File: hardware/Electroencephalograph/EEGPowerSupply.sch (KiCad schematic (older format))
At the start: 25 parts, among them U10 TC1017-xCT, U11 TPS60403, U8 TC1017-xCT, U9 TC1017-xCT

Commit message: enqable separate electrodes for each point
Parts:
- added C62: 100n, Capacitor_SMD:C_0402_1005Metric, symbol Device:C
- added L4, L5: 3u3, Inductor_SMD:L_1206_3216Metric, symbol Device:L
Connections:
- wire segments 85 -> 90
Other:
- moved on the sheet: C71, TP4, TP6
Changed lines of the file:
@@
 $Descr A4 11693 8268
 encoding utf-8
-Sheet 6 6
+Sheet 6 7
 Title ""
 Date ""
@@
 AR Path="/5DFE0AD6/5E0A0C58" Ref="U?"  Part="1"
 AR Path="/5E0992D6/5E0A0C58" Ref="U11"  Part="1"
-F 0 "U11" H 3750 5750 50  0000 L CNN
-F 1 "TPS60403" H 3650 5650 50  0000 L CNN
+F 0 "U11" H 3550 5800 50  0000 L CNN
+F 1 "TPS60403" H 3550 5700 50  0000 L CNN
 F 2 "Package_SO:SOP-8_3.76x4.96mm_P1.27mm" H 5050 5650 50  0001 C CNN
 F 3 "" H 5050 5650 50  0001 C CNN
@@
 L Device:CP C?
 U 1 1 5E0A0CA0
-P 4250 5200
+P 4400 5200
 AR Path="/5DF4CFF8/5E0A0CA0" Ref="C?"  Part="1"
 AR Path="/5DF61103/5E0A0CA0" Ref="C?"  Part="1"
 AR Path="/5DFE0AD6/5E0A0CA0" Ref="C?"  Part="1"
 AR Path="/5E0992D6/5E0A0CA0" Ref="C71"  Part="1"
-F 0 "C71" H 4368 5246 50  0000 L CNN
-F 1 "22u" H 4368 5155 50  0000 L CNN
-F 2 "Capacitor_Tantalum_SMD:CP_EIA-3528-21_Kemet-B" H 4288 5050 50  0001 C CNN
-F 3 "~" H 4250 5200 50  0001 C CNN
-	1    4250 5200
+F 0 "C71" H 4518 5246 50  0000 L CNN
+F 1 "22u" H 4518 5155 50  0000 L CNN
+F 2 "Capacitor_Tantalum_SMD:CP_EIA-3528-21_Kemet-B" H 4438 5050 50  0001 C CNN
+F 3 "~" H 4400 5200 50  0001 C CNN
+	1    4400 5200
 	1    0    0    1
 $EndComp
@@
 Connection ~ 2700 5500
 Wire Wire Line
-	3850 5500 4250 5500
-Wire Wire Line
-	4250 5500 4250 5350
-Connection ~ 3850 5500
+	4400 5500 4400 5350
 $Comp
 L Electroencephalograph:A_GND #PWR?
 U 1 1 5E0A0CB3
-P 4250 5000
+P 4400 5000
 AR Path="/5DFE0AD6/5E0A0CB3" Ref="#PWR?"  Part="1"
 AR Path="/5E0992D6/5E0A0CB3" Ref="#PWR117"  Part="1"
-F 0 "#PWR117" H 4250 5025 50  0001 C CNN
-F 1 "A_GND" H 4267 4827 50  0000 C CNN
-F 2 "" H 4250 5025 50  0001 C CNN
-F 3 "" H 4250 5025 50  0001 C CNN
-	1    4250 5000
-	1    0    0    1
-$EndComp
-Wire Wire Line
-	4250 5000 4250 5050
+F 0 "#PWR117" H 4400 5025 50  0001 C CNN
+F 1 "A_GND" H 4417 4827 50  0000 C CNN
+F 2 "" H 4400 5025 50  0001 C CNN
+F 3 "" H 4400 5025 50  0001 C CNN
+	1    4400 5000
+	1    0    0    1
+$EndComp
+Wire Wire Line
+	4400 5000 4400 5050
 $Comp
 L Device:C C?
@@
 	6550 5000 6550 5100
 Wire Wire Line
-	4250 5500 5350 5500
-Connection ~ 4250 5500
+	4400 5500 5350 5500
+Connection ~ 4400 5500
 Wire Wire Line
 	6550 5500 6550 5400
@@
 $EndComp
 $Comp
-L Device:C C?
-U 1 1 5E104488
-P 6600 2750
-AR Path="/5DF4CFF8/5E104488" Ref="C?"  Part="1"
-AR Path="/5DF61103/5E104488" Ref="C?"  Part="1"
-AR Path="/5DFE0AD6/5E104488" Ref="C?"  Part="1"
-AR Path="/5E0992D6/5E104488" Ref="C61"  Part="1"
-F 0 "C61" H 6715 2796 50  0000 L CNN
-F 1 "1u" H 6715 2705 50  0000 L CNN
-F 2 "Capacitor_SMD:C_0402_1005Metric" H 6638 2600 50  0001 C CNN
-F 3 "~" H 6600 2750 50  0001 C CNN
-	1    6600 2750
-	1    0    0    -1
-$EndComp
-$Comp
 L Electroencephalograph:D_GND #PWR?
 U 1 1 5E10486F
@@
 	1    0    0    -1
 $EndComp
-$Comp
-L Electroencephalograph:D_GND #PWR?
-U 1 1 5E108919
-P 6600 3000
-AR Path="/5DFE0AD6/5E108919" Ref="#PWR?"  Part="1"
-AR Path="/5E0992D6/5E108919" Ref="#PWR107"  Part="1"
-F 0 "#PWR107" H 6600 3025 50  0001 C CNN
-F 1 "D_GND" H 6617 2827 50  0000 C CNN
-F 2 "" H 6600 3025 50  0001 C CNN
-F 3 "" H 6600 3025 50  0001 C CNN
-	1    6600 3000
-	1    0    0    -1
-$EndComp
 Wire Wire Line
 	5500 2400 5350 2400
@@
 	6000 2800 6000 3000
 Wire Wire Line
-	6400 2400 6600 2400
-Wire Wire Line
-	6600 2400 6600 2600
-Wire Wire Line
-	6600 2900 6600 3000
-Wire Wire Line
-	6600 2400 8300 2400
-Wire Wire Line
 	8300 2400 8300 2250
-Connection ~ 6600 2400
 Wire Wire Line
 	5350 2400 2050 2400
@@
 L Connector:TestPoint TP?
 U 1 1 5E19CD08
-P 6600 2300
+P 7100 2300
 AR Path="/5DF61103/5E19CD08" Ref="TP?"  Part="1"
 AR Path="/5E0992D6/5E19CD08" Ref="TP4"  Part="1"
-F 0 "TP4" H 6658 2418 50  0000 L CNN
-F 1 "TestPoint" H 6658 2327 50  0000 L CNN
-F 2 "TestPoint:TestPoint_Pad_1.5x1.5mm" H 6800 2300 50  0001 C CNN
-F 3 "~" H 6800 2300 50  0001 C CNN
-	1    6600 2300
-	1    0    0    -1
-$EndComp
-Wire Wire Line
-	6600 2300 6600 2400
+F 0 "TP4" H 7158 2418 50  0000 L CNN
+F 1 "TestPoint" H 7158 2327 50  0000 L CNN
+F 2 "TestPoint:TestPoint_Pad_1.5x1.5mm" H 7300 2300 50  0001 C CNN
+F 3 "~" H 7300 2300 50  0001 C CNN
+	1    7100 2300
+	1    0    0    -1
+$EndComp
 $Comp
 L Connector:TestPoint TP?
@@
 L Connector:TestPoint TP?
 U 1 1 5E1AE8F5
-P 4250 5600
+P 4400 5600
 AR Path="/5DF61103/5E1AE8F5" Ref="TP?"  Part="1"
 AR Path="/5E0992D6/5E1AE8F5" Ref="TP6"  Part="1"
-F 0 "TP6" H 4192 5626 50  0000 R CNN
-F 1 "TestPoint" H 4192 5717 50  0000 R CNN
-F 2 "TestPoint:TestPoint_Pad_1.5x1.5mm" H 4450 5600 50  0001 C CNN
-F 3 "~" H 4450 5600 50  0001 C CNN
-	1    4250 5600
+F 0 "TP6" H 4342 5626 50  0000 R CNN
+F 1 "TestPoint" H 4342 5717 50  0000 R CNN
+F 2 "TestPoint:TestPoint_Pad_1.5x1.5mm" H 4600 5600 50  0001 C CNN
+F 3 "~" H 4600 5600 50  0001 C CNN
+	1    4400 5600
 	-1   0    0    1
 $EndComp
 Wire Wire Line
-	4250 5600 4250 5500
+	4400 5600 4400 5500
+$Comp
+L Device:L L?
+U 1 1 5DFF5B3E
+P 4100 5500
+AR Path="/5DFE0AD6/5DFF5B3E" Ref="L?"  Part="1"
+AR Path="/5E0992D6/5DFF5B3E" Ref="L5"  Part="1"
+F 0 "L5" V 4290 5500 50  0000 C CNN
+F 1 "3u3" V 4199 5500 50  0000 C CNN
+F 2 "Inductor_SMD:L_1206_3216Metric" H 4100 5500 50  0001 C CNN
+F 3 "~" H 4100 5500 50  0001 C CNN
+	1    4100 5500
+	0    1    1    0
+$EndComp
+$Comp
+L Device:C C?
+U 1 1 5DFFE643
+P 6550 2650
+AR Path="/5DF4CFF8/5DFFE643" Ref="C?"  Part="1"
+AR Path="/5DF61103/5DFFE643" Ref="C?"  Part="1"
+AR Path="/5DFE0AD6/5DFFE643" Ref="C?"  Part="1"
+AR Path="/5E0992D6/5DFFE643" Ref="C61"  Part="1"
+F 0 "C61" H 6665 2696 50  0000 L CNN
+F 1 "1u" H 6665 2605 50  0000 L CNN
+F 2 "Capacitor_SMD:C_0402_1005Metric" H 6588 2500 50  0001 C CNN
+F 3 "~" H 6550 2650 50  0001 C CNN
+	1    6550 2650
+	1    0    0    -1
+$EndComp
+$Comp
+L Electroencephalograph:A_GND #PWR?
+U 1 1 5DFFE649
+P 6550 2900
+AR Path="/5DFE0AD6/5DFFE649" Ref="#PWR?"  Part="1"
+AR Path="/5E0992D6/5DFFE649" Ref="#PWR107"  Part="1"
+F 0 "#PWR107" H 6550 2925 50  0001 C CNN
+F 1 "A_GND" H 6567 2727 50  0000 C CNN
+F 2 "" H 6550 2925 50  0001 C CNN
+F 3 "" H 6550 2925 50  0001 C CNN
+	1    6550 2900
+	1    0    0    -1
+$EndComp
+Wire Wire Line
+	6550 2900 6550 2800
+Wire Wire Line
+	6550 2400 6550 2500
+$Comp
+L Device:L L?
+U 1 1 5DFFE651
+P 6850 2400
+AR Path="/5DFE0AD6/5DFFE651" Ref="L?"  Part="1"
+AR Path="/5E0992D6/5DFFE651" Ref="L4"  Part="1"
+F 0 "L4" V 7040 2400 50  0000 C CNN
+F 1 "3u3" V 6949 2400 50  0000 C CNN
+F 2 "Inductor_SMD:L_1206_3216Metric" H 6850 2400 50  0001 C CNN
+F 3 "~" H 6850 2400 50  0001 C CNN
+	1    6850 2400
+	0    -1   -1   0
+$EndComp
+$Comp
+L Device:C C?
+U 1 1 5DFFE657
+P 7100 2650
+AR Path="/5DF4CFF8/5DFFE657" Ref="C?"  Part="1"
+AR Path="/5DF61103/5DFFE657" Ref="C?"  Part="1"
+AR Path="/5DFE0AD6/5DFFE657" Ref="C?"  Part="1"
+AR Path="/5E0992D6/5DFFE657" Ref="C62"  Part="1"
+F 0 "C62" H 7215 2696 50  0000 L CNN
+F 1 "100n" H 7215 2605 50  0000 L CNN
+F 2 "Capacitor_SMD:C_0402_1005Metric" H 7138 2500 50  0001 C CNN
+F 3 "~" H 7100 2650 50  0001 C CNN
+	1    7100 2650
+	1    0    0    -1
+$EndComp
+Wire Wire Line
+	6550 2400 6700 2400
+Connection ~ 6550 2400
+Wire Wire Line
+	7000 2400 7100 2400
+Wire Wire Line
+	7100 2400 7100 2500
+$Comp
+L Electroencephalograph:A_GND #PWR?
+U 1 1 5DFFE661
+P 7100 2900
+AR Path="/5DFE0AD6/5DFFE661" Ref="#PWR?"  Part="1"
+AR Path="/5E0992D6/5DFFE661" Ref="#PWR121"  Part="1"
+F 0 "#PWR121" H 7100 2925 50  0001 C CNN
+F 1 "A_GND" H 7117 2727 50  0000 C CNN
+F 2 "" H 7100 2925 50  0001 C CNN
+F 3 "" H 7100 2925 50  0001 C CNN
+	1    7100 2900
+	1    0    0    -1
+$EndComp
+Wire Wire Line
+	7100 2900 7100 2800
+Connection ~ 7100 2400
+Wire Wire Line
+	6400 2400 6550 2400
+Wire Wire Line
+	7100 2400 8300 2400
+Wire Wire Line
+	7100 2300 7100 2400
+Wire Wire Line
+	3850 5500 3950 5500
+Connection ~ 3850 5500
+Wire Wire Line
+	4250 5500 4400 5500
 $EndSCHEMATC

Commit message: removed external clk and vref
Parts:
- removed L2, L3, L4: 3u3, Inductor_SMD:L_1206_3216Metric, symbol Device:L
- removed U10, U8, U9: TC1017-xCT, Package_TO_SOT_SMD:SOT-23-5, symbol Regulator_Linear:TC1017-xCT
- added L5: 22u, Inductor_SMD:L_1206_3216Metric, symbol Device:L
- added TP8: TestPoint, TestPoint:TestPoint_Pad_1.5x1.5mm, symbol Connector:TestPoint
- added U6, U7, U9: LP5912-1.8DRVT, symbol Electroencephalograph:LP5912-1.8DRVT
- C56: renamed from C61; value 1u -> 2u2
- C58: renamed from C60; value 1u -> 2u2
- C59: renamed from C63; value 1u -> 2u2
- C61: renamed from C64; value 1u -> 2u2
- C66: renamed from C72; value 1u -> 2u2
- C68: renamed from C67; value 22u -> 100u
- C69: value 1u -> 2u2
- L6: renamed from L5; value 3u3 -> 22u
- renumbered C62 to C57, C55 to C60, C57 to C62, C58 to C63, C70 to C64, C71 to C65, C68 to C67, C59 to C70, C65 to C71, TP5 to TP10, TP6 to TP11, TP7 to TP12, TP4 to TP9, U11 to U8
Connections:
- wire segments 90 -> 107
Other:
- note added: "Power Supply (TP8) = 5V\nD_VDD (TP9) = 1V8\nA_VDD (TP10) = 1V8\nA_VSS (TP12) = -1V8\nvoltage inverter output (TP11) =-4V5"
- moved on the sheet: C56, C57, C58, C59, C60, C61, C62, C63, C64, C65, C66, C67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

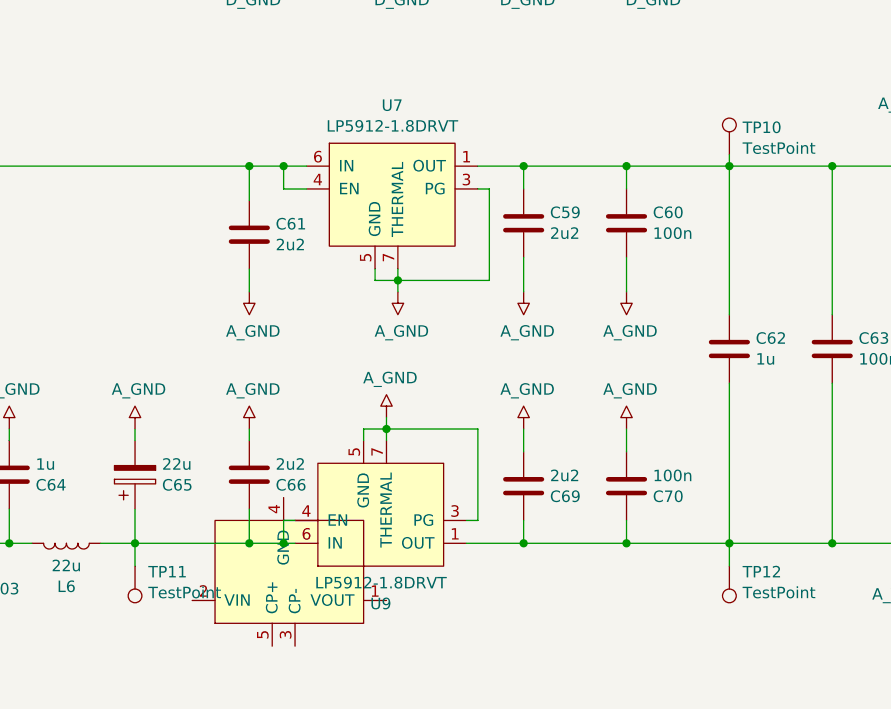
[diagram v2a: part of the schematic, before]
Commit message: bom simplification
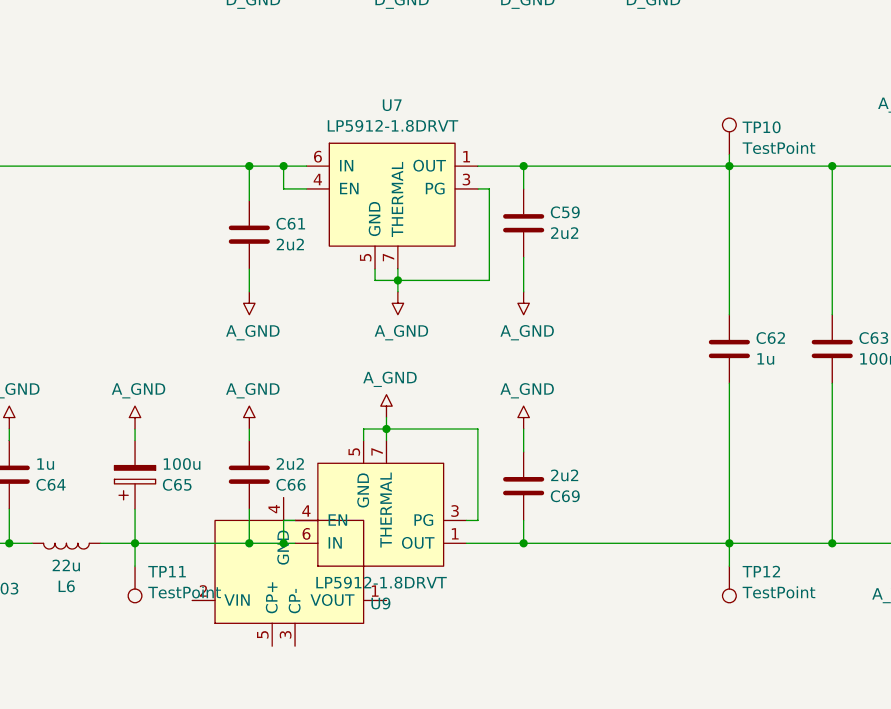
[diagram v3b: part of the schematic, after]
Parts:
- removed C60, C70: 100n, Capacitor_SMD:C_0402_1005Metric, symbol Device:C
- C65: value 22u -> 100u
- C68: footprint Capacitor_Tantalum_SMD:CP_EIA-3528-21_Kemet-B -> Capacitor_SMD:CP_Elec_6.3x5.8
- L5, L6: footprint Inductor_SMD:L_1206_3216Metric -> Inductor_SMD:L_7.3x7.3_H3.5
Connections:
- wire segments 107 -> 101
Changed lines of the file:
@@
 F 0 "C68" H 2882 5296 50  0000 R CNN
 F 1 "100u" H 2882 5205 50  0000 R CNN
-F 2 "Capacitor_Tantalum_SMD:CP_EIA-3528-21_Kemet-B" H 3038 5100 50  0001 C CNN
+F 2 "Capacitor_SMD:CP_Elec_6.3x5.8" H 3038 5100 50  0001 C CNN
 F 3 "~" H 3000 5250 50  0001 C CNN
 	1    3000 5250
@@
 AR Path="/5E0992D6/5E0A0CA0" Ref="C65"  Part="1"
 F 0 "C65" H 4918 5246 50  0000 L CNN
-F 1 "22u" H 4918 5155 50  0000 L CNN
+F 1 "100u" H 4918 5155 50  0000 L CNN
 F 2 "Capacitor_Tantalum_SMD:CP_EIA-3528-21_Kemet-B" H 4838 5050 50  0001 C CNN
 F 3 "~" H 4800 5200 50  0001 C CNN
@@
 	1    0    0    -1
 $EndComp
-$Comp
-L Device:C C?
-U 1 1 5E0CDD1B
-P 6950 4100
-AR Path="/5DF4CFF8/5E0CDD1B" Ref="C?"  Part="1"
-AR Path="/5DF61103/5E0CDD1B" Ref="C?"  Part="1"
-AR Path="/5DFE0AD6/5E0CDD1B" Ref="C?"  Part="1"
-AR Path="/5E0992D6/5E0CDD1B" Ref="C60"  Part="1"
-F 0 "C60" H 7065 4146 50  0000 L CNN
-F 1 "100n" H 7065 4055 50  0000 L CNN
-F 2 "Capacitor_SMD:C_0402_1005Metric" H 6988 3950 50  0001 C CNN
-F 3 "~" H 6950 4100 50  0001 C CNN
-	1    6950 4100
-	1    0    0    -1
-$EndComp
 Connection ~ 6500 3850
-Wire Wire Line
-	6950 3850 6950 3950
-$Comp
-L Electroencephalograph:A_GND #PWR?
-U 1 1 5E0CF637
-P 6950 4400
-AR Path="/5DFE0AD6/5E0CF637" Ref="#PWR?"  Part="1"
-AR Path="/5E0992D6/5E0CF637" Ref="#PWR117"  Part="1"
-F 0 "#PWR117" H 6950 4425 50  0001 C CNN
-F 1 "A_GND" H 6967 4227 50  0000 C CNN
-F 2 "" H 6950 4425 50  0001 C CNN
-F 3 "" H 6950 4425 50  0001 C CNN
-	1    6950 4400
-	1    0    0    -1
-$EndComp
-Wire Wire Line
-	6950 4400 6950 4250
-Wire Wire Line
-	6950 3850 7400 3850
-Connection ~ 6950 3850
-$Comp
-L Device:C C?
-U 1 1 5E0D898C
-P 6950 5250
-AR Path="/5DF4CFF8/5E0D898C" Ref="C?"  Part="1"
-AR Path="/5DF61103/5E0D898C" Ref="C?"  Part="1"
-AR Path="/5DFE0AD6/5E0D898C" Ref="C?"  Part="1"
-AR Path="/5E0992D6/5E0D898C" Ref="C70"  Part="1"
-F 0 "C70" H 7065 5296 50  0000 L CNN
-F 1 "100n" H 7065 5205 50  0000 L CNN
-F 2 "Capacitor_SMD:C_0402_1005Metric" H 6988 5100 50  0001 C CNN
-F 3 "~" H 6950 5250 50  0001 C CNN
-	1    6950 5250
-	1    0    0    1
-$EndComp
-Wire Wire Line
-	6950 5500 6950 5400
-$Comp
-L Electroencephalograph:A_GND #PWR?
-U 1 1 5E0D8994
-P 6950 5000
-AR Path="/5DFE0AD6/5E0D8994" Ref="#PWR?"  Part="1"
-AR Path="/5E0992D6/5E0D8994" Ref="#PWR126"  Part="1"
-F 0 "#PWR126" H 6950 5025 50  0001 C CNN
-F 1 "A_GND" H 6967 4827 50  0000 C CNN
-F 2 "" H 6950 5025 50  0001 C CNN
-F 3 "" H 6950 5025 50  0001 C CNN
-	1    6950 5000
-	1    0    0    1
-$EndComp
-Wire Wire Line
-	6950 5000 6950 5100
-Wire Wire Line
-	6950 5500 7400 5500
 Wire Wire Line
 	7400 3850 7850 3850
@@
 F 0 "L6" V 4690 5500 50  0000 C CNN
 F 1 "22u" V 4599 5500 50  0000 C CNN
-F 2 "Inductor_SMD:L_1206_3216Metric" H 4500 5500 50  0001 C CNN
+F 2 "Inductor_SMD:L_7.3x7.3_H3.5" H 4500 5500 50  0001 C CNN
 F 3 "~" H 4500 5500 50  0001 C CNN
 	1    4500 5500
@@
 F 0 "L5" V 2890 5500 50  0000 C CNN
 F 1 "22u" V 2799 5500 50  0000 C CNN
-F 2 "Inductor_SMD:L_1206_3216Metric" H 2700 5500 50  0001 C CNN
+F 2 "Inductor_SMD:L_7.3x7.3_H3.5" H 2700 5500 50  0001 C CNN
 F 3 "~" H 2700 5500 50  0001 C CNN
 	1    2700 5500
@@
 	2850 5500 3000 5500
 Connection ~ 3000 5500
-Wire Wire Line
-	6500 3850 6950 3850
 Wire Wire Line
 	6500 2400 7050 2400
@@
 Wire Wire Line
 	6250 5500 6500 5500
-Wire Wire Line
-	6500 5500 6950 5500
 Connection ~ 6500 5500
-Connection ~ 6950 5500
 $Comp
 L Connector:TestPoint TP?
@@
 	2400 2050 2400 1950
 Connection ~ 2050 2050
+Wire Wire Line
+	6500 5500 7400 5500
+Wire Wire Line
+	6500 3850 7400 3850
 $EndSCHEMATC

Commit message: draft of PCB routing
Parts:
- renumbered C67 to C56, C68 to C57, C71 to C58, C64 to C59, C65 to C60, C58 to C61, C61 to C62, C66 to C63, C56 to C64, C59 to C65, C69 to C66, C57 to C67, C62 to C68, C63 to C69, TP11 to TP10, TP9 to TP11, TP10 to TP12, TP12 to TP13, TP8 to TP9, U8 to U6, U9 to U7, U6 to U8, U7 to U9

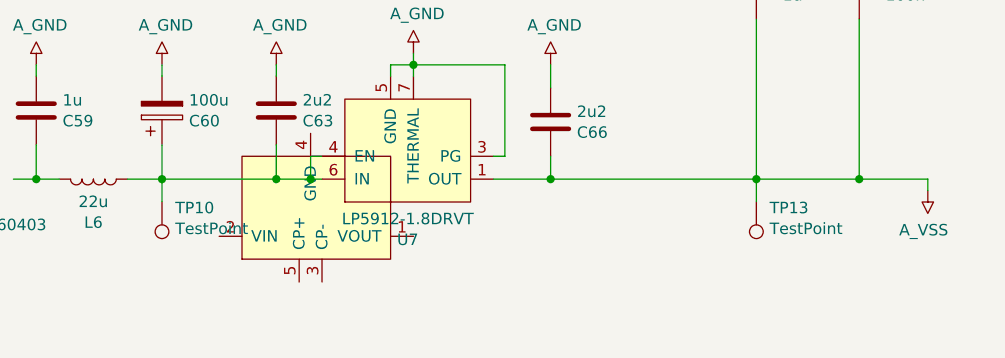
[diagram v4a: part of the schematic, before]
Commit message: added inductor 3d model
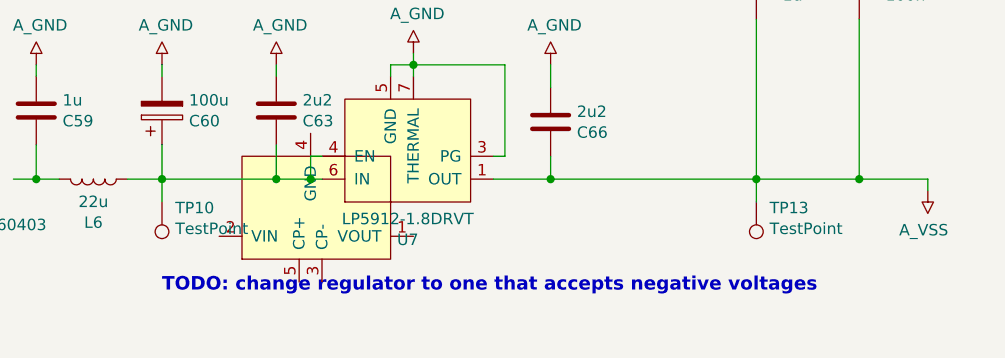
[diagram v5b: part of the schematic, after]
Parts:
- L5, L6: footprint Inductor_SMD:L_7.3x7.3_H3.5 -> Electroencephalograph:L_7.3x7.3_H3.5
- U7, U8, U9: footprint (none) -> Package_SON:WSON-8-1EP_2x2mm_P0.5mm_EP0.9x1.6mm_ThermalVias
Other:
- note added: "TODO: change regulator to one that accepts negative voltages"
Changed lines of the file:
@@
 F 0 "L6" V 4690 5500 50  0000 C CNN
 F 1 "22u" V 4599 5500 50  0000 C CNN
-F 2 "Inductor_SMD:L_7.3x7.3_H3.5" H 4500 5500 50  0001 C CNN
+F 2 "Electroencephalograph:L_7.3x7.3_H3.5" H 4500 5500 50  0001 C CNN
 F 3 "~" H 4500 5500 50  0001 C CNN
 	1    4500 5500
@@
 F 0 "L5" V 2890 5500 50  0000 C CNN
 F 1 "22u" V 2799 5500 50  0000 C CNN
-F 2 "Inductor_SMD:L_7.3x7.3_H3.5" H 2700 5500 50  0001 C CNN
+F 2 "Electroencephalograph:L_7.3x7.3_H3.5" H 2700 5500 50  0001 C CNN
 F 3 "~" H 2700 5500 50  0001 C CNN
 	1    2700 5500
@@
 F 0 "U8" H 5925 2365 50  0000 C CNN
 F 1 "LP5912-1.8DRVT" H 5925 2274 50  0000 C CNN
-F 2 "" H 5950 2250 50  0001 C CNN
+F 2 "Package_SON:WSON-8-1EP_2x2mm_P0.5mm_EP0.9x1.6mm_ThermalVias" H 5950 2250 50  0001 C CNN
 F 3 "" H 5950 2250 50  0001 C CNN
 	1    5950 2250
@@
 F 0 "U9" H 5925 3815 50  0000 C CNN
 F 1 "LP5912-1.8DRVT" H 5925 3724 50  0000 C CNN
-F 2 "" H 5950 3700 50  0001 C CNN
+F 2 "Package_SON:WSON-8-1EP_2x2mm_P0.5mm_EP0.9x1.6mm_ThermalVias" H 5950 3700 50  0001 C CNN
 F 3 "" H 5950 3700 50  0001 C CNN
 	1    5950 3700
@@
 F 0 "U7" H 5875 5765 50  0000 C CNN
 F 1 "LP5912-1.8DRVT" H 5875 5674 50  0000 C CNN
-F 2 "" H 5900 5650 50  0001 C CNN
+F 2 "Package_SON:WSON-8-1EP_2x2mm_P0.5mm_EP0.9x1.6mm_ThermalVias" H 5900 5650 50  0001 C CNN
 F 3 "" H 5900 5650 50  0001 C CNN
 	1    5900 5650
@@
 Wire Wire Line
 	6500 3850 7400 3850
+Text Notes 4800 6000 0    59   ~ 12
+TODO: change regulator to one that accepts negative voltages
 $EndSCHEMATC

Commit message: placing power supply on pcb
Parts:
- C60: footprint Capacitor_Tantalum_SMD:CP_EIA-3528-21_Kemet-B -> Capacitor_SMD:CP_Elec_6.3x5.8
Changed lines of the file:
@@
 F 0 "C60" H 4918 5246 50  0000 L CNN
 F 1 "100u" H 4918 5155 50  0000 L CNN
-F 2 "Capacitor_Tantalum_SMD:CP_EIA-3528-21_Kemet-B" H 4838 5050 50  0001 C CNN
+F 2 "Capacitor_SMD:CP_Elec_6.3x5.8" H 4838 5050 50  0001 C CNN
 F 3 "~" H 4800 5200 50  0001 C CNN
 	1    4800 5200
